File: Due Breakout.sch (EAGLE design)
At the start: 1 part

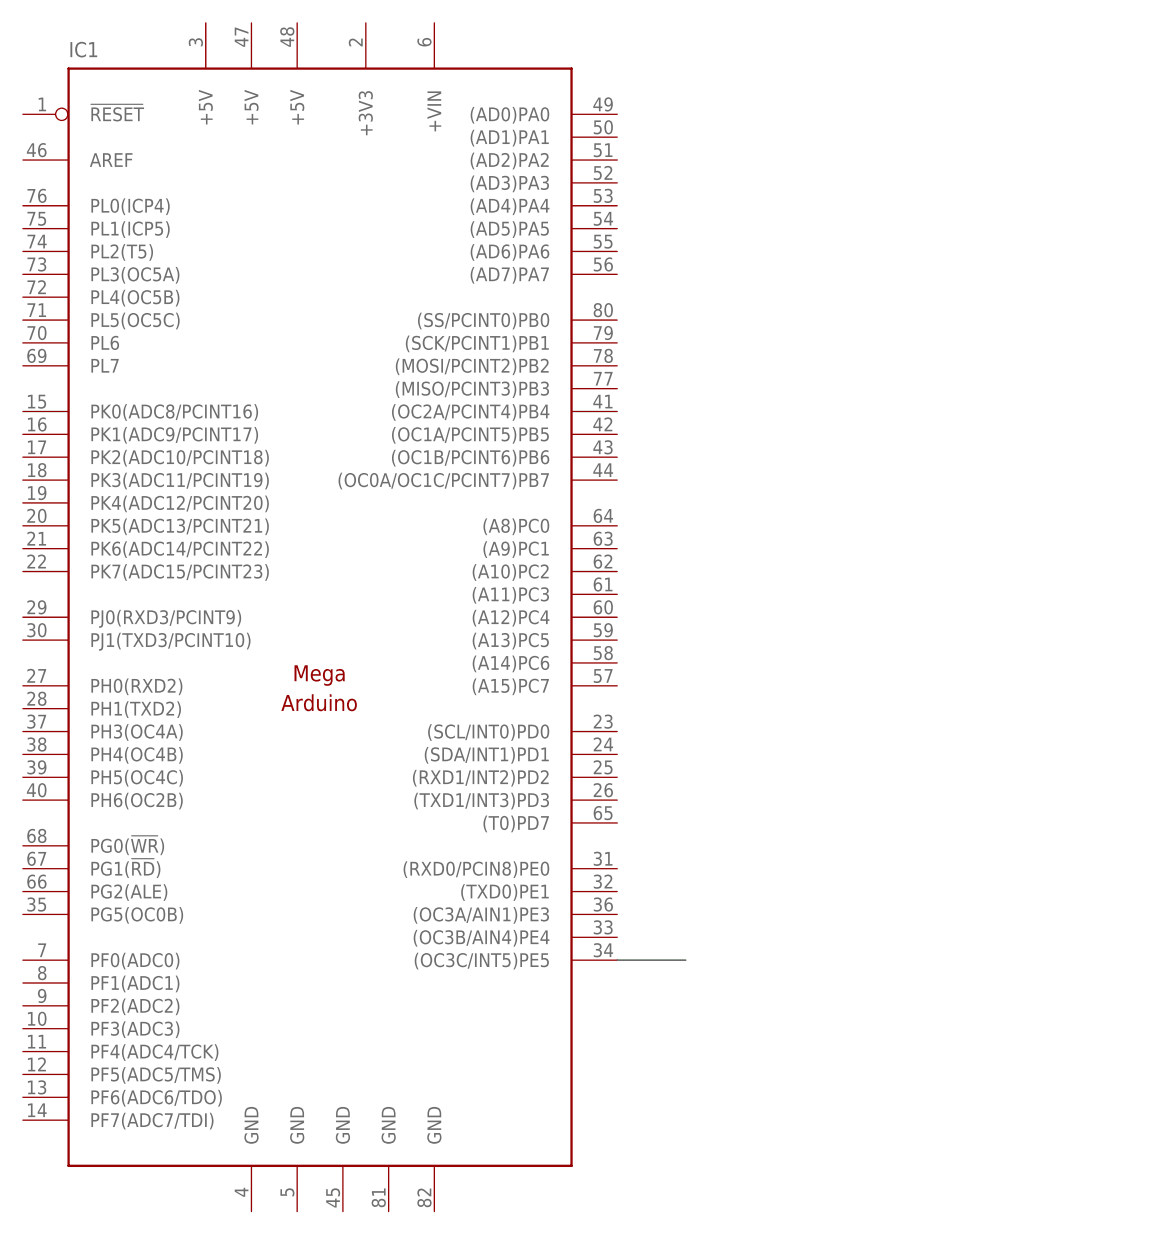
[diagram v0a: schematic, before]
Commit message: Add 8-header pin schematic
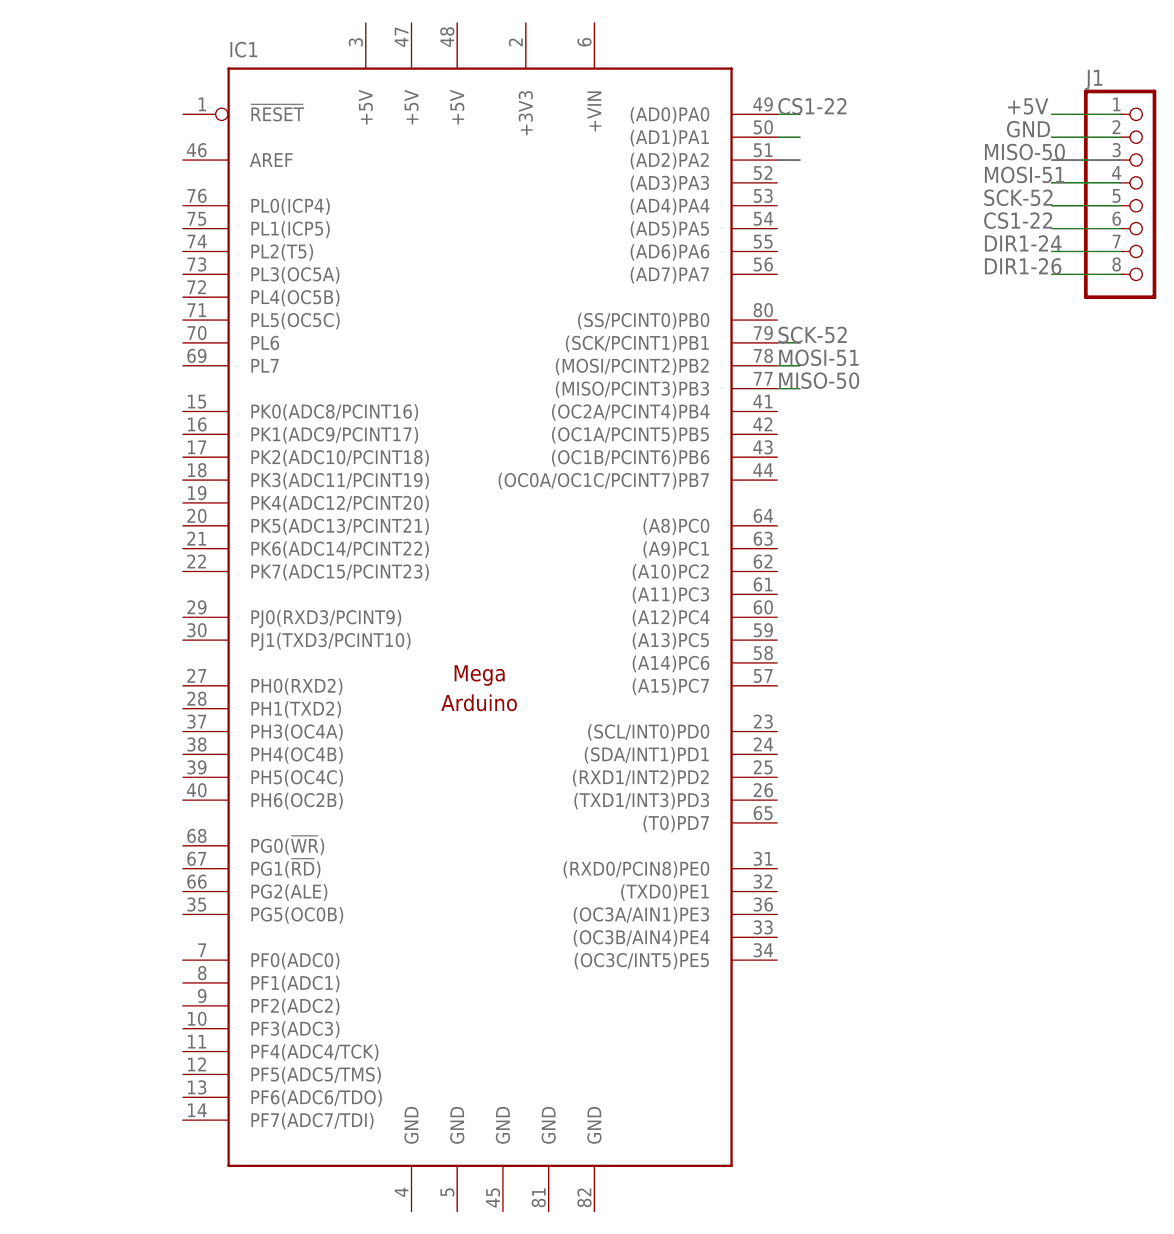
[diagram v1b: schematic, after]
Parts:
- added J1: (no value), pinhead:PINHD-1X8
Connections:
- removed net 4: IC1.(OC3C/INT5)PE5
- new net +5V: J1.1
- new net CS1-22: IC1.(AD0)PA0, J1.6
- new net DIR1-24: J1.7
- new net DIR1-26: J1.8
- new net GND: J1.2
- new net MISO-50: IC1.(MISO/PCINT3)PB3, J1.3
- new net MOSI-51: IC1.(MOSI/PCINT2)PB2, J1.4
- new net N$1: IC1.(AD1)PA1
- new net N$2: IC1.(AD2)PA2
- new net SCK-52: IC1.(SCK/PCINT1)PB1, J1.5
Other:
- moved on the sheet: IC1
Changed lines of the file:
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@@
 <parts>
 <part name="IC1" library="arduino" deviceset="MEGAARDUINO_1" device=""/>
+<part name="J1" library="pinhead" library_urn="urn:adsk.eagle:library:325" deviceset="PINHD-1X8" device="" package3d_urn="urn:adsk.eagle:package:22409/2"/>
 </parts>
 <sheets>
@@
 </plain>
 <instances>
-<instance part="IC1" gate="G$1" x="73.66" y="40.64" smashed="yes">
-<attribute name="NAME" x="45.72" y="110.49" size="1.6764" layer="95"/>
+<instance part="IC1" gate="G$1" x="91.44" y="40.64" smashed="yes">
+<attribute name="NAME" x="63.5" y="110.49" size="1.6764" layer="95"/>
+</instance>
+<instance part="J1" gate="A" x="165.1" y="93.98" smashed="yes">
+<attribute name="NAME" x="158.75" y="107.315" size="1.778" layer="95"/>
+<attribute name="VALUE" x="158.75" y="81.28" size="1.778" layer="96"/>
 </instance>
 </instances>
@@
 </busses>
 <nets>
-<net name="4" class="0">
+<net name="CS1-22" class="0">
 <segment>
-<pinref part="IC1" gate="G$1" pin="(OC3C/INT5)PE5"/>
-<wire x1="106.68" y1="10.16" x2="114.3" y2="10.16" width="0.1524" layer="91"/>
+<pinref part="J1" gate="A" pin="6"/>
+<wire x1="162.56" y1="91.44" x2="154.94" y2="91.44" width="0.1524" layer="91"/>
+<label x="147.32" y="91.44" size="1.778" layer="95"/>
+</segment>
+<segment>
+<pinref part="IC1" gate="G$1" pin="(AD0)PA0"/>
+<wire x1="124.46" y1="104.14" x2="127" y2="104.14" width="0.1524" layer="91"/>
+<label x="124.46" y="104.14" size="1.778" layer="95"/>
+</segment>
+</net>
+<net name="DIR1-24" class="0">
+<segment>
+<pinref part="J1" gate="A" pin="7"/>
+<wire x1="162.56" y1="88.9" x2="154.94" y2="88.9" width="0.1524" layer="91"/>
+<label x="147.32" y="88.9" size="1.778" layer="95"/>
+</segment>
+</net>
+<net name="DIR1-26" class="0">
+<segment>
+<pinref part="J1" gate="A" pin="8"/>
+<wire x1="162.56" y1="86.36" x2="154.94" y2="86.36" width="0.1524" layer="91"/>
+<label x="147.32" y="86.36" size="1.778" layer="95"/>
+</segment>
+</net>
+<net name="+5V" class="0">
+<segment>
+<pinref part="J1" gate="A" pin="1"/>
+<wire x1="162.56" y1="104.14" x2="154.94" y2="104.14" width="0.1524" layer="91"/>
+<label x="149.86" y="104.14" size="1.778" layer="95"/>
+</segment>
+</net>
+<net name="GND" class="0">
+<segment>
+<pinref part="J1" gate="A" pin="2"/>
+<wire x1="162.56" y1="101.6" x2="154.94" y2="101.6" width="0.1524" layer="91"/>
+<label x="149.86" y="101.6" size="1.778" layer="95"/>
+</segment>
+</net>
+<net name="MISO-50" class="0">
+<segment>
+<pinref part="J1" gate="A" pin="3"/>
+<wire x1="162.56" y1="99.06" x2="154.94" y2="99.06" width="0.1524" layer="91"/>
+<label x="147.32" y="99.06" size="1.778" layer="95"/>
+</segment>
+<segment>
+<pinref part="IC1" gate="G$1" pin="(MISO/PCINT3)PB3"/>
+<wire x1="124.46" y1="73.66" x2="127" y2="73.66" width="0.1524" layer="91"/>
+<label x="124.46" y="73.66" size="1.778" layer="95"/>
+</segment>
+</net>
+<net name="MOSI-51" class="0">
+<segment>
+<pinref part="J1" gate="A" pin="4"/>
+<wire x1="162.56" y1="96.52" x2="154.94" y2="96.52" width="0.1524" layer="91"/>
+<label x="147.32" y="96.52" size="1.778" layer="95"/>
+</segment>
+<segment>
+<pinref part="IC1" gate="G$1" pin="(MOSI/PCINT2)PB2"/>
+<wire x1="124.46" y1="76.2" x2="127" y2="76.2" width="0.1524" layer="91"/>
+<label x="124.46" y="76.2" size="1.778" layer="95"/>
+</segment>
+</net>
+<net name="SCK-52" class="0">
+<segment>
+<pinref part="J1" gate="A" pin="5"/>
+<wire x1="162.56" y1="93.98" x2="154.94" y2="93.98" width="0.1524" layer="91"/>
+<label x="147.32" y="93.98" size="1.778" layer="95"/>
+</segment>
+<segment>
+<pinref part="IC1" gate="G$1" pin="(SCK/PCINT1)PB1"/>
+<wire x1="124.46" y1="78.74" x2="127" y2="78.74" width="0.1524" layer="91"/>
+<label x="124.46" y="78.74" size="1.778" layer="95"/>
+</segment>
+</net>
+<net name="N$1" class="0">
+<segment>
+<pinref part="IC1" gate="G$1" pin="(AD1)PA1"/>
+<wire x1="124.46" y1="101.6" x2="127" y2="101.6" width="0.1524" layer="91"/>
+</segment>
+</net>
+<net name="N$2" class="0">
+<segment>
+<pinref part="IC1" gate="G$1" pin="(AD2)PA2"/>
+<wire x1="124.46" y1="99.06" x2="127" y2="99.06" width="0.1524" layer="91"/>
 </segment>
 </net>
@@
 </schematic>
 </drawing>
+<compatibility>
+<note version="8.2" severity="warning">
+Since Version 8.2, EAGLE supports online libraries. The ids
+of those online libraries will not be understood (or retained)
+with this version.
+</note>
+<note version="8.3" severity="warning">
+Since Version 8.3, EAGLE supports URNs for individual library
+assets (packages, symbols, and devices). The URNs of those assets
+will not be understood (or retained) with this version.
+</note>
+<note version="8.3" severity="warning">
+Since Version 8.3, EAGLE supports the association of 3D packages
+with devices in libraries, schematics, and board files. Those 3D
+packages will not be understood (or retained) with this version.
+</note>
+</compatibility>
 </eagle>
